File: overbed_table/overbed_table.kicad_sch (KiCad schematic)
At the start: 35 parts, among them CN10 DLL-5569-2AW, CN2 KF2EDGRC-5.08-4P, CN3 KF2EDGRC-5.08-4P, CN8 DLL-5569-2AW, CN9 DLL-5569-2AW, SW1 KH-6X6X6H-STM, SW2 KH-6X6X6H-STM, U1 AP2112K-3.3TRG1, U2 ESP32-C3-WROOM-02, U3 WAFER-XH254WZ-2A, U4 BSMD2920-500-24V, U5 BSMD2920-500-24V, U6 BSMD2920-500-24V, U7 KF7620-7.62-2P, X1 AFA01-S05FCA-00

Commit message: update: 更新主板电源指示灯
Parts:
- added D3: LED, LED_SMD:LED_0603_1608Metric, symbol Device:LED
- added R11: 10k, Resistor_SMD:R_0603_1608Metric, symbol PCM_SparkFun-Resistor:R
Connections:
- net +12V: now also D3.2 (A)
- net GND: now also R11.2
- new net: D3.1 (K), R11.1

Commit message: update: 添加主板测试点
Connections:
- net GND: no longer X1.6, X1.7
- no-connect marks 4 -> 6
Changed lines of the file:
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@@
-	)
-	(junction
-		(at 104.14 85.09)
-		(diameter 0)
-		(color 0 0 0 0)
 	)
 	(junction
@@
 	)
 	(junction
-		(at 96.52 85.09)
-		(diameter 0)
-		(color 0 0 0 0)
-	)
-	(junction
 		(at 247.65 60.96)
 		(diameter 0)
@@
 		(diameter 0)
 		(color 0 0 0 0)
+	)
+	(no_connect
+		(at 96.52 78.74)
+	)
+	(no_connect
+		(at 96.52 58.42)
 	)
 	(no_connect
@@
 	(wire
 		(pts
-			(xy 104.14 85.09) (xy 177.8 85.09)
-		)
-		(stroke
-			(width 0)
-			(type default)
-		)
-	)
-	(wire
-		(pts
 			(xy 80.01 124.46) (xy 80.01 129.54)
 		)
@@
 	(wire
 		(pts
-			(xy 96.52 58.42) (xy 96.52 55.88)
-		)
-		(stroke
-			(width 0)
-			(type default)
-		)
-	)
-	(wire
-		(pts
 			(xy 247.65 90.17) (xy 247.65 140.97)
 		)
@@
 	(wire
 		(pts
-			(xy 96.52 55.88) (xy 104.14 55.88)
-		)
-		(stroke
-			(width 0)
-			(type default)
-		)
-	)
-	(wire
-		(pts
 			(xy 34.29 181.61) (xy 34.29 184.15)
 		)
@@
 	(wire
 		(pts
-			(xy 104.14 55.88) (xy 104.14 85.09)
-		)
-		(stroke
-			(width 0)
-			(type default)
-		)
-	)
-	(wire
-		(pts
 			(xy 147.32 50.8) (xy 162.56 50.8)
 		)
@@
 	(wire
 		(pts
-			(xy 96.52 78.74) (xy 96.52 85.09)
-		)
-		(stroke
-			(width 0)
-			(type default)
-		)
-	)
-	(wire
-		(pts
 			(xy 87.63 158.75) (xy 87.63 160.02)
 		)
@@
 	(wire
 		(pts
-			(xy 67.31 85.09) (xy 104.14 85.09)
-		)
-		(stroke
+			(xy 67.31 85.09) (xy 177.8 85.09)
+		)
+		(stroke

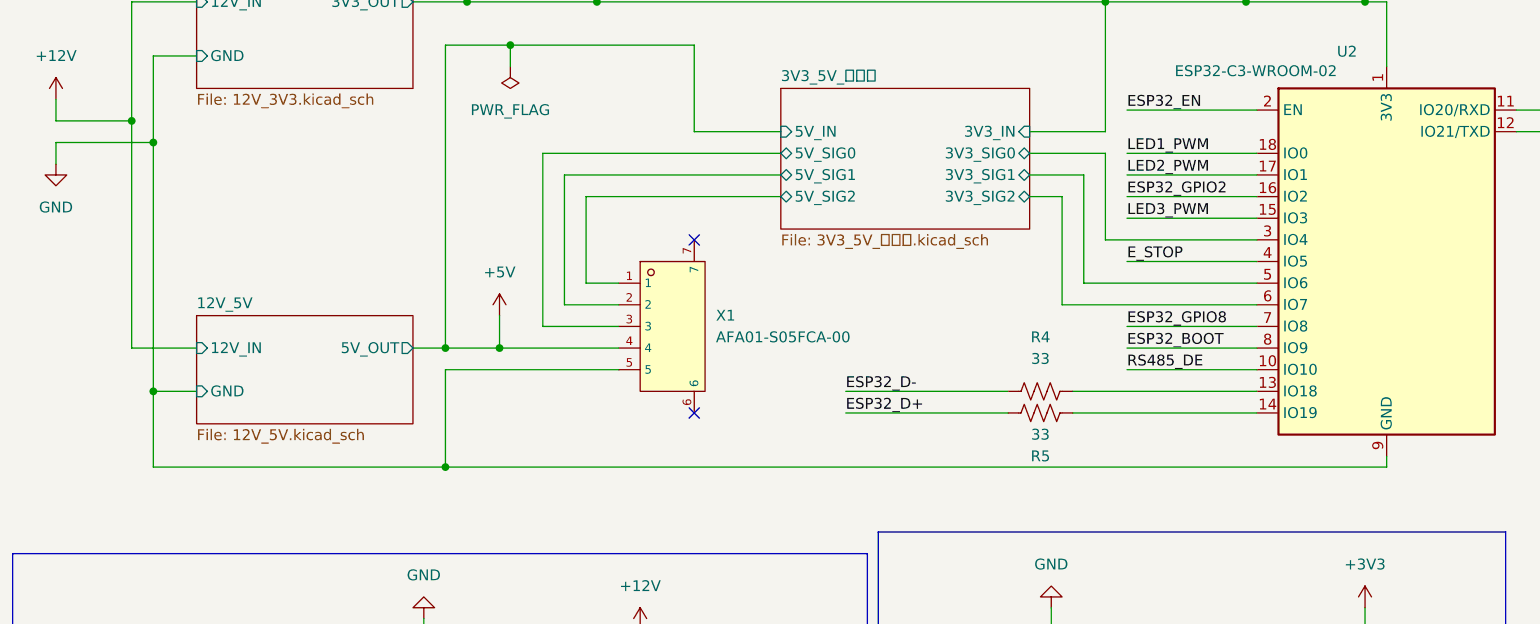
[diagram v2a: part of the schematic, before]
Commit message: update: 更新按钮小板设计，导出gerber文件
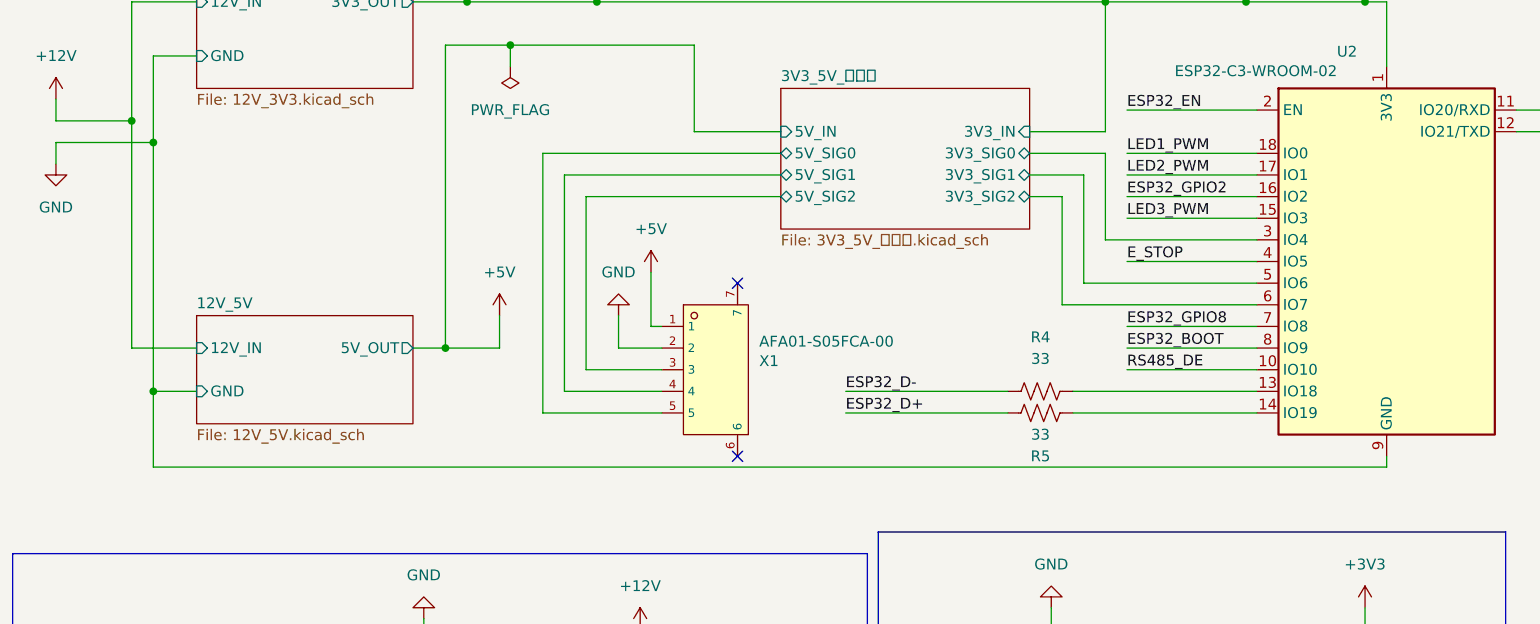
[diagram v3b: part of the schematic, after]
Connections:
- net +5V: now also X1.1; no longer X1.4
- net 3V3_5V_转换器/5V_SIG0: now also X1.5; no longer X1.3
- net 3V3_5V_转换器/5V_SIG1: now also X1.4; no longer X1.2
- net 3V3_5V_转换器/5V_SIG2: now also X1.3; no longer X1.1
- net GND: now also X1.2; no longer X1.5
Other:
- moved on the sheet: X1
